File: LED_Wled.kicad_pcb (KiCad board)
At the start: 2 copper layers, 77.5 x 29 mm, 48 parts, among them J1 SWD_PORT_SKEDD, J2 Barrel_Jack, J3 VIN-Out, J4 Microphone input, J5 LED_signal_chan, J6 +5V Out, Q1 AO4485, Q2 AO4485, Q3 MMBT3904, Q4 AO4485, Q5 AO4485, U1 ESP32-WROOM-32, U2 TPS5450DDAR, U3 AMS1117-3.3, U4 SN74HC125DR

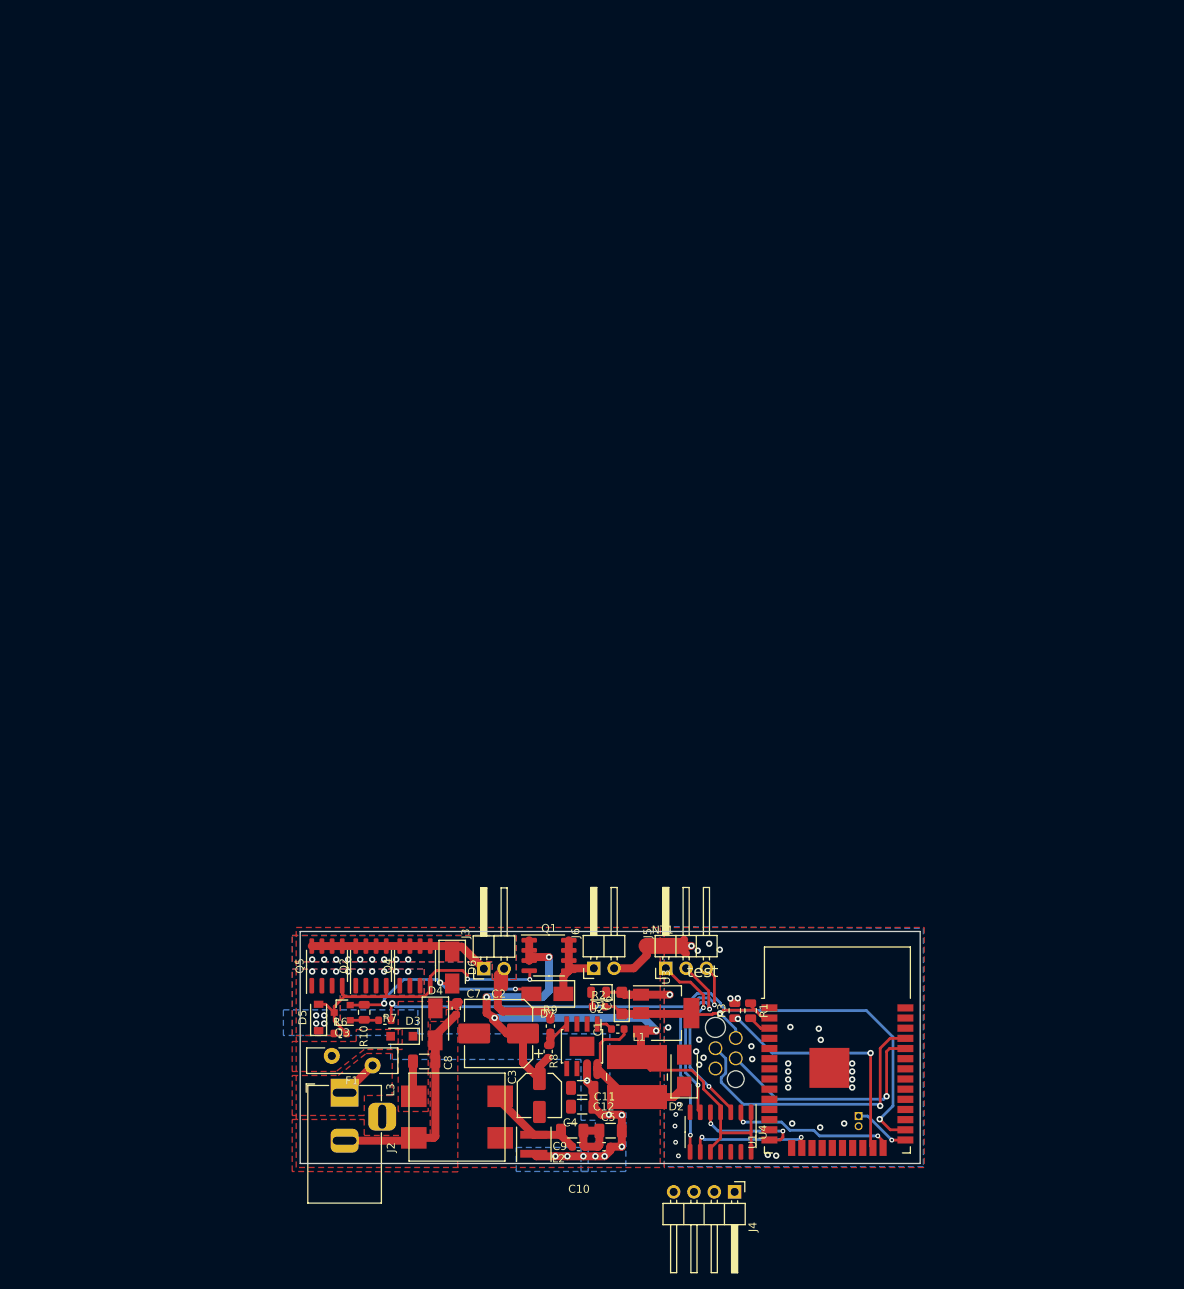
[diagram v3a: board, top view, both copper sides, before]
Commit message: redrawn pcb from scratch rev2.0
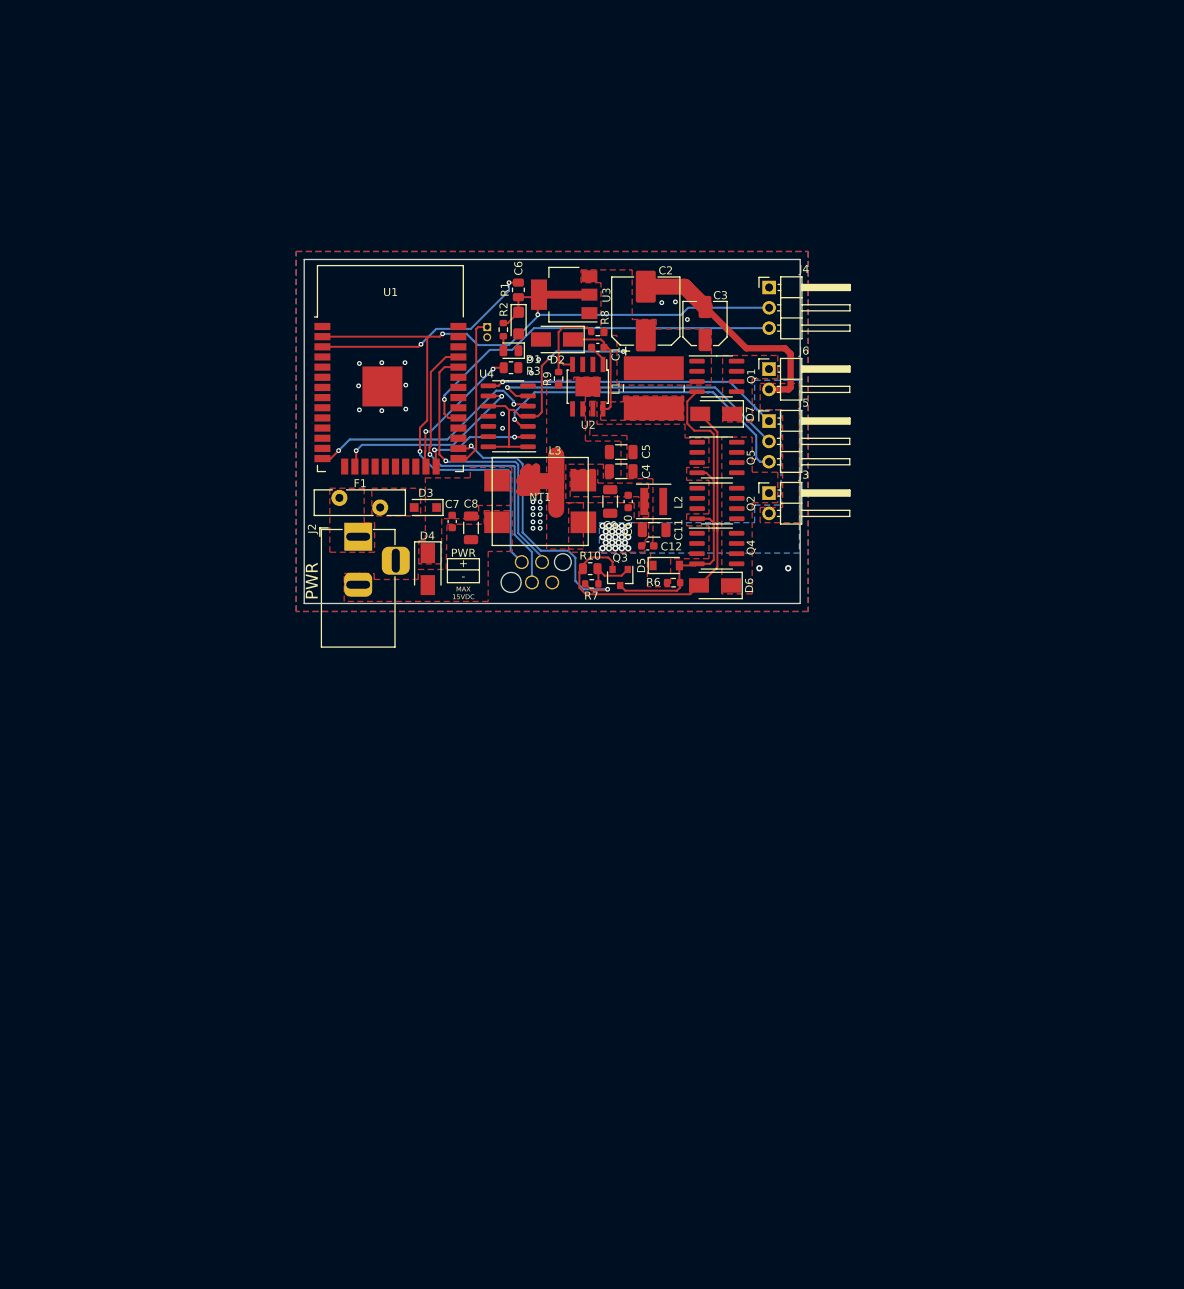
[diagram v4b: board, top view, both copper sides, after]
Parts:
- added G***: LOGO, LED_Wled:es, B.Cu at (143.8, 98.0)
- J4: value Microphone input -> MIC_input; footprint Connector_PinHeader_2.54mm:PinHeader_1x04_P2.54mm_Horizontal -> Connector_PinHeader_2.54mm:PinHeader_1x03_P2.54mm_Horizontal
- moved J4 113.1 mm to (160.1, 79.5), turned to 0 degrees
- moved BOOT1 109.0 mm to (124.9, 84.5)
- moved U1 101.9 mm to (112.8, 92.6)
- moved C3 98.7 mm to (152.1, 84.0), turned to 90 degrees
- moved R1 94.7 mm to (128.8, 79.8), turned to 90 degrees
- moved U4 93.3 mm to (127.5, 95.6), turned to 180 degrees
- moved D2 92.8 mm to (133.6, 86.0), turned to 180 degrees
- moved C2 92.2 mm to (144.7, 82.5), turned to 90 degrees
- moved U3 90.7 mm to (134.5, 80.4), turned to 180 degrees
- moved R8 90.2 mm to (138.7, 85.0), turned to 180 degrees
- moved L1 86.1 mm to (145.7, 92.1)
- moved C6 86.0 mm to (128.8, 84.0), turned to 270 degrees
- moved R2 85.5 mm to (126.9, 84.8), turned to 90 degrees
- moved C1 85.2 mm to (138.7, 87.0)
- moved R3 85.1 mm to (127.9, 89.5), turned to 0 degrees
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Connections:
- J4 pad 3: +3V3 -> MIC
- J5 pad 1: LED_OUT_HS1 -> LED_OUT_HS3
- J5 pad 3: LED_OUT_HS3 -> LED_OUT_HS1
- U1 pad 10: (no net) -> Net-(U1-Pad10)
- U1 pad 11: (no net) -> Net-(U1-Pad11)
- U1 pad 12: (no net) -> Net-(U1-Pad12)
- U1 pad 13: (no net) -> Net-(U1-Pad13)
- U1 pad 17: (no net) -> Net-(U1-Pad17)
- U1 pad 18: (no net) -> Net-(U1-Pad18)
- U1 pad 19: (no net) -> Net-(U1-Pad19)
- U1 pad 20: (no net) -> Net-(U1-Pad20)
- U1 pad 21: (no net) -> Net-(U1-Pad21)
- U1 pad 22: (no net) -> Net-(U1-Pad22)
- U1 pad 27: (no net) -> Net-(U1-Pad27)
- U1 pad 28: (no net) -> Net-(U1-Pad28)
- U1 pad 30: (no net) -> Net-(U1-Pad30)
- U1 pad 31: (no net) -> Net-(U1-Pad31)
- U1 pad 32: (no net) -> Net-(U1-Pad32)
- U1 pad 33: (no net) -> Net-(U1-Pad33)
- U1 pad 36: (no net) -> Net-(U1-Pad36)
- U1 pad 37: (no net) -> Net-(U1-Pad37)
- U1 pad 4: (no net) -> Net-(U1-Pad4)
- U1 pad 5: (no net) -> Net-(U1-Pad5)
- U1 pad 6: (no net) -> Net-(U1-Pad6)
- U1 pad 7: (no net) -> Net-(U1-Pad7)
- U1 pad 8: (no net) -> Net-(U1-Pad8)
- U1 pad 9: (no net) -> Net-(U1-Pad9)
- U2 pad 2: (no net) -> Net-(U2-Pad2)
- U2 pad 3: (no net) -> Net-(U2-Pad3)
- U2 pad 5: (no net) -> Net-(U2-Pad5)
- U4 pad 11: (no net) -> Net-(U4-Pad11)
- U4 pad 12: (no net) -> Net-(U4-Pad12)
- U4 pad 13: (no net) -> GND
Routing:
- net +3V3: track 26.9 -> 113.8 mm, vias 1 -> 3
- net +5V: track 89.9 -> 33.7 mm, vias 4 -> 2
- net MIC: track 0.00 -> 48.4 mm, vias 0 -> 1
- net LED_VOUT_SWS: track 82.7 -> 36.1 mm
- net VBat-: track 30.8 -> 0.00 mm
- net Vin: track 25.6 -> 0.00 mm, vias 22 -> 0
- net Net-(R1-Pad2): track 2.87 -> 28.4 mm, vias 0 -> 2
- net LED_VOUT: track 23.2 -> 0.00 mm, vias 9 -> 0
- net Net-(D6-Pad2): track 26.4 -> 47.6 mm, vias 3 -> 0
- net LED_OUT_HS1: track 23.5 -> 41.2 mm, vias 2 -> 1
- net LED_OUT_LS2: track 13.5 -> 30.2 mm
- net LED_OUT_HS2: track 23.3 -> 38.5 mm, vias 2 -> 1
- net Net-(R3-Pad1): track 30.8 -> 17.5 mm
- net Net-(C10-Pad2): track 12.5 -> 0.00 mm
- net Net-(BOOT1-Pad1): track 7.10 -> 19.2 mm, vias 1 -> 0
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- added copper zone on F.Cu, net +5V
- added copper zone on B.Cu, net GNDPWR
- added copper zone on F.Cu, net LED_5VOUT
- added copper zone on F.Cu, net Net-(C1-Pad1)
- added copper zone on F.Cu, net Net-(C10-Pad2)
- removed copper zone on B.Cu, net LED_VOUT
- removed copper zone on B.Cu, net Vin
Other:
- board size 77.5 x 29 mm -> 62 x 43 mm
- board text added: "+ -"
- board text added: "ESled-Controller 2022-07-22 rev2.0"
- board text added: "MAX 15VDC"
- board text added: "PWR"
- board text removed: "test"

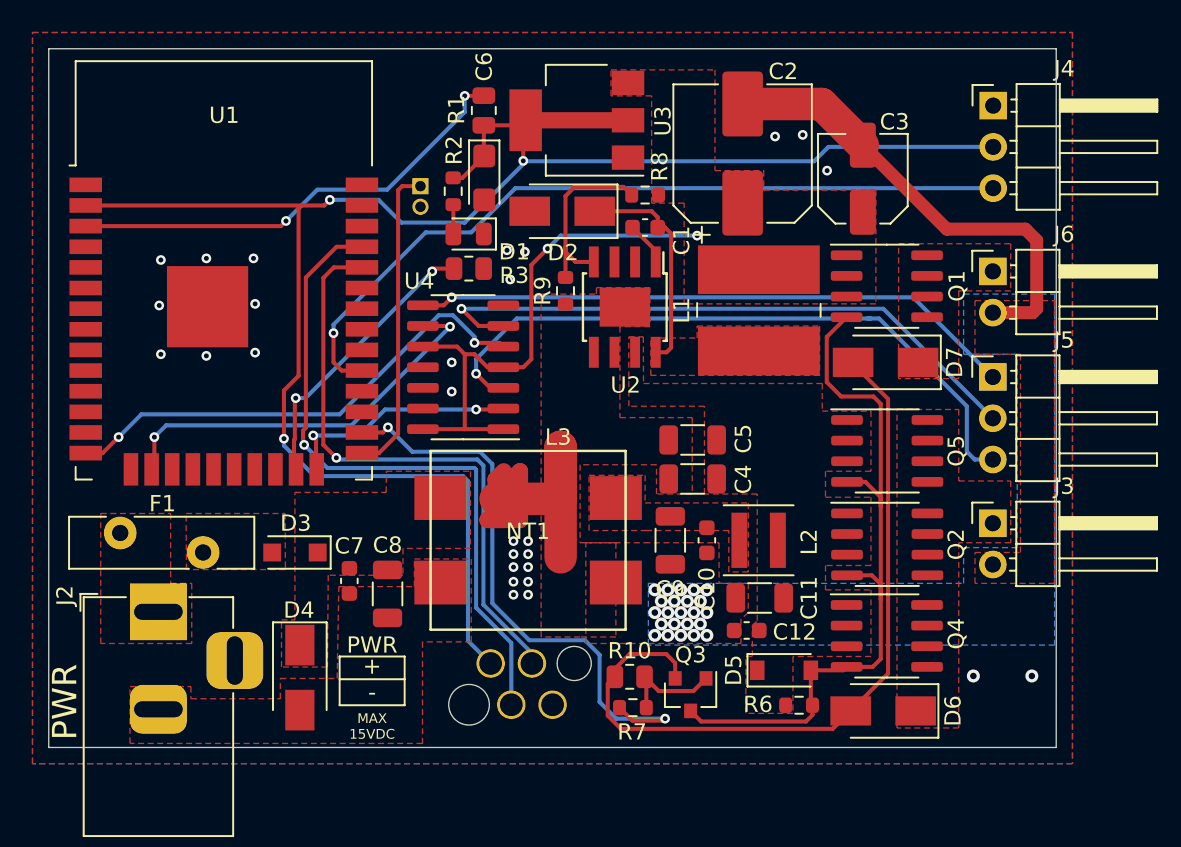
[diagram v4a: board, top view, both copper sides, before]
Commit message: fixed +5v rail switch
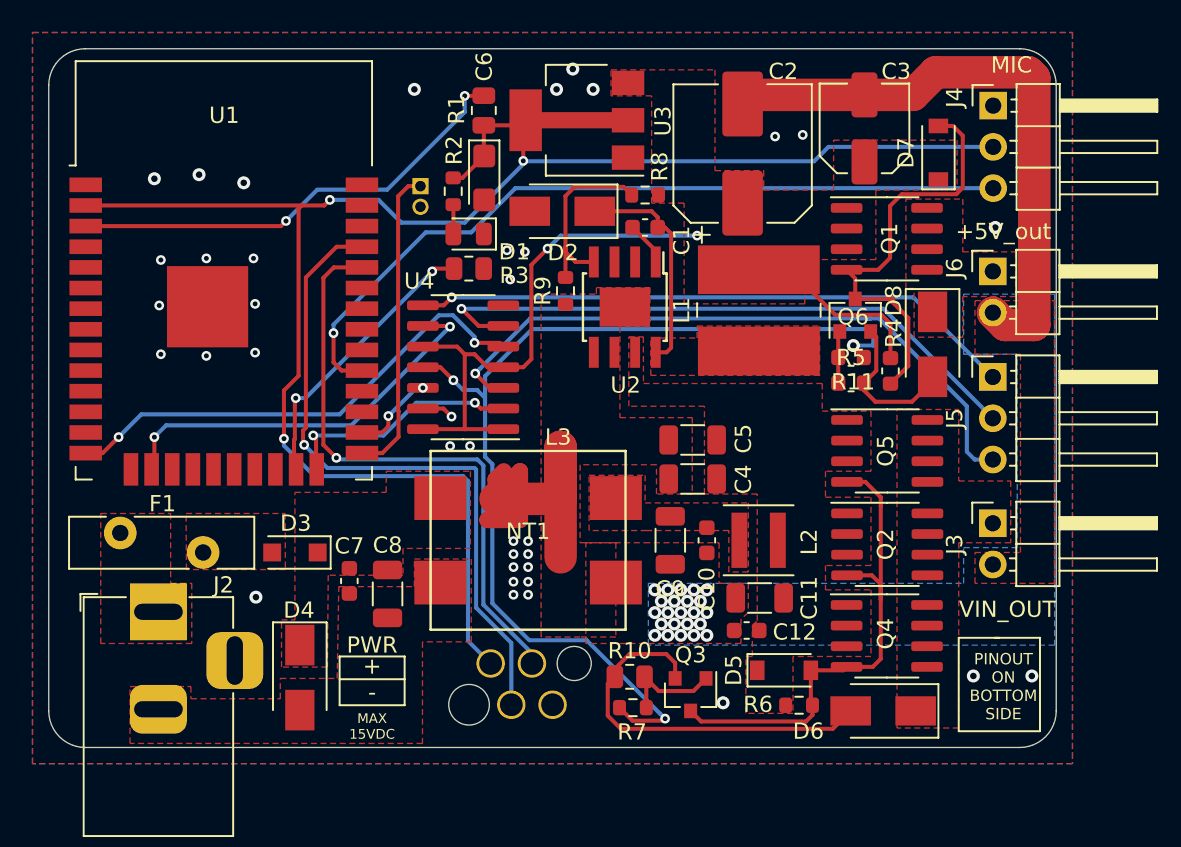
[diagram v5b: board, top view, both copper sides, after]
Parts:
- added D8: SS34, Diode_SMD:D_SMA, F.Cu at (156.4, 94.2)
- added G***: LOGO, userdvc:pepe-soldering, B.Cu at (128.0, 98.2)
- added Q6: MMBT3904, Package_TO_SOT_SMD:SOT-23, F.Cu at (151.6, 92.4)
- added R11: 10k, Resistor_SMD:R_0603_1608Metric, F.Cu at (151.4, 96.6)
- added R4: 4.7k, Resistor_SMD:R_0603_1608Metric, F.Cu at (153.8, 95.8)
- added R5: 1k, Resistor_SMD:R_0603_1608Metric, F.Cu at (151.4, 95.0)
- D7: value SS34 -> BZT52B15; footprint Diode_SMD:D_SMA -> Diode_SMD:D_SOD-123
- moved D7 13.3 mm to (156.8, 82.4), turned to 90 degrees
- moved G*** 4.09 mm to (139.8, 98.5), turned to 90 degrees
- moved C3 3.10 mm to (152.2, 80.9)
- moved Q1 2.91 mm to (153.6, 87.7)
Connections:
- D7 pad 1: LED_5VOUT -> +5V
- D7 pad 2: Net-(D6-Pad2) -> Net-(D7-Pad2)
- Q1 pad 4: Net-(D5-Pad2) -> Net-(D7-Pad2)
- R7 pad 2: LED_VOUT_SWS -> LED_VOUT_HSWS
- U1 pad 10: Net-(U1-Pad10) -> (no net)
- U1 pad 11: Net-(U1-Pad11) -> (no net)
- U1 pad 12: Net-(U1-Pad12) -> (no net)
- U1 pad 13: Net-(U1-Pad13) -> (no net)
- U1 pad 17: Net-(U1-Pad17) -> (no net)
- U1 pad 18: Net-(U1-Pad18) -> (no net)
- U1 pad 19: Net-(U1-Pad19) -> (no net)
- U1 pad 20: Net-(U1-Pad20) -> (no net)
- U1 pad 21: Net-(U1-Pad21) -> (no net)
- U1 pad 22: Net-(U1-Pad22) -> (no net)
- U1 pad 26: LED_VOUT_SWS -> LED_VOUT_LSWS
- U1 pad 27: Net-(U1-Pad27) -> (no net)
- U1 pad 28: Net-(U1-Pad28) -> (no net)
- U1 pad 30: Net-(U1-Pad30) -> (no net)
- U1 pad 31: Net-(U1-Pad31) -> (no net)
- U1 pad 32: Net-(U1-Pad32) -> (no net)
- U1 pad 33: Net-(U1-Pad33) -> (no net)
- U1 pad 36: Net-(U1-Pad36) -> (no net)
- U1 pad 37: Net-(U1-Pad37) -> (no net)
- U1 pad 4: Net-(U1-Pad4) -> (no net)
- U1 pad 5: Net-(U1-Pad5) -> (no net)
- U1 pad 6: Net-(U1-Pad6) -> (no net)
- U1 pad 7: Net-(U1-Pad7) -> (no net)
- U1 pad 8: Net-(U1-Pad8) -> (no net)
- U1 pad 9: Net-(U1-Pad9) -> (no net)
- U2 pad 2: Net-(U2-Pad2) -> (no net)
- U2 pad 3: Net-(U2-Pad3) -> (no net)
- U2 pad 5: Net-(U2-Pad5) -> (no net)
- U4 pad 11: Net-(U4-Pad11) -> LED_VOUT_HSWS
- U4 pad 12: Net-(U4-Pad12) -> LED_VOUT_LSWS
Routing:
- net LED_VOUT_HSWS: track 0.00 -> 63.8 mm, vias 0 -> 3
- net LED_VOUT_SWS: track 36.1 -> 0.00 mm, vias 2 -> 0
- net Net-(D7-Pad2): track 0.00 -> 26.6 mm
- net Net-(D6-Pad2): track 47.6 -> 24.1 mm
- net Net-(D5-Pad2): track 45.7 -> 31.0 mm
- net +5V: track 33.7 -> 45.3 mm
- net Net-(D8-Pad2): track 0.00 -> 9.39 mm
- net GNDPWR: track 38.6 -> 47.0 mm
- net LED_VOUT_LSWS: track 0.00 -> 5.26 mm, vias 0 -> 2
- net Net-(Q6-Pad1): track 0.00 -> 3.21 mm
- net GND: track 10.8 -> 12.8 mm, vias 28 -> 38
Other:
- outline, holes or cut-outs redrawn
- board text added: "+3V3"
- board text added: "+5V_OUT"
- board text added: "+5V_out"
- board text added: "ESled-Controller 2022-11-16 rev2.0"
- board text added: "GND"
- board text added: "LED1"
- board text added: "LED2"
- board text added: "LED3"
- board text added: "MIC"
- board text added: "PINOUT ON BOTTOM SIDE"
- board text added: "VIN_OUT"
- board text added: "VOUT"
- board text removed: "ESled-Controller 2022-07-22 rev2.0"

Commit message: migration to kicad 6
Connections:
- U1 pad 10: (no net) -> unconnected-(U1-Pad10)
- U1 pad 11: (no net) -> unconnected-(U1-Pad11)
- U1 pad 12: (no net) -> unconnected-(U1-Pad12)
- U1 pad 13: (no net) -> unconnected-(U1-Pad13)
- U1 pad 17: (no net) -> unconnected-(U1-Pad17)
- U1 pad 18: (no net) -> unconnected-(U1-Pad18)
- U1 pad 19: (no net) -> unconnected-(U1-Pad19)
- U1 pad 20: (no net) -> unconnected-(U1-Pad20)
- U1 pad 21: (no net) -> unconnected-(U1-Pad21)
- U1 pad 22: (no net) -> unconnected-(U1-Pad22)
- U1 pad 27: (no net) -> unconnected-(U1-Pad27)
- U1 pad 28: (no net) -> unconnected-(U1-Pad28)
- U1 pad 30: (no net) -> unconnected-(U1-Pad30)
- U1 pad 31: (no net) -> unconnected-(U1-Pad31)
- U1 pad 32: (no net) -> unconnected-(U1-Pad32)
- U1 pad 33: (no net) -> unconnected-(U1-Pad33)
- U1 pad 36: (no net) -> unconnected-(U1-Pad36)
- U1 pad 37: (no net) -> unconnected-(U1-Pad37)
- U1 pad 4: (no net) -> unconnected-(U1-Pad4)
- U1 pad 5: (no net) -> unconnected-(U1-Pad5)
- U1 pad 6: (no net) -> unconnected-(U1-Pad6)
- U1 pad 7: (no net) -> unconnected-(U1-Pad7)
- U1 pad 8: (no net) -> unconnected-(U1-Pad8)
- U1 pad 9: (no net) -> unconnected-(U1-Pad9)
- U2 pad 2: (no net) -> unconnected-(U2-Pad2)
- U2 pad 3: (no net) -> unconnected-(U2-Pad3)
- U2 pad 5: (no net) -> unconnected-(U2-Pad5)
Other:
- net class Default removed

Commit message: updated parts, rdy for production?
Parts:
- removed the G*** at (128.0, 98.2)
- L1: footprint Inductor_SMD:L_Wuerth_WE-PD2-Typ-L -> Inductor_SMD:L_Wuerth_WE-PD2-Typ-XL
- L2: footprint Inductor_SMD:L_Coilcraft_XxL4030 -> Inductor_SMD:L_Bourns_SRP7028A_7.3x6.6mm
- moved C12 6.31 mm to (146.3, 118.0)
- moved C11 5.98 mm to (143.7, 115.4), turned to 90 degrees
- moved C5 5.71 mm to (136.5, 97.5)
- moved L2 3.18 mm to (145.2, 109.4)
- moved C4 2.38 mm to (141.7, 100.1)
- moved C2 1.84 mm to (144.3, 80.7), turned to 0 degrees
- moved R7 1.63 mm to (136.9, 117.8)
- moved Q3 1.63 mm to (140.4, 117.0)
- moved R10 1.63 mm to (136.7, 115.9)
- moved C10 1.44 mm to (142.7, 104.8), turned to 180 degrees
- moved L1 1.43 mm to (145.1, 90.8)
- moved C9 1.28 mm to (139.9, 105.0)
- moved R11 1.07 mm to (152.4, 96.3), turned to 90 degrees
- moved Q6 0.69 mm to (152.2, 92.1)
- moved Q1 0.63 mm to (154.2, 87.7)
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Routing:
- net GND: track 12.8 -> 31.0 mm, vias 38 -> 33
- net GNDPWR: track 47.0 -> 58.7 mm, vias 23 -> 22
- net Net-(C10-Pad2): track 0.00 -> 10.3 mm
- net Vin: track 0.00 -> 3.73 mm
- net Net-(Q6-Pad1): track 3.21 -> 6.10 mm, vias 0 -> 2
- net LED_VOUT_HSWS: track 63.8 -> 61.3 mm
- net Net-(D5-Pad2): track 31.0 -> 32.8 mm, vias 0 -> 2
- net Net-(D8-Pad2): track 9.39 -> 8.07 mm
- net Net-(D6-Pad2): track 24.1 -> 22.8 mm, vias 0 -> 2
- net RXD: track 37.6 -> 36.7 mm
- net Net-(D7-Pad2): track 26.6 -> 25.7 mm
- net Net-(C1-Pad1): track 13.7 -> 12.9 mm
